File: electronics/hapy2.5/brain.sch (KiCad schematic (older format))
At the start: 37 parts, among them P10 WTemp probe, P11 LED Red Lower, P12 WCycle Lower, P13 WCycle Upper, P14 LED Red Upper, P15 Air probe, P16 LED White Upper, P17 LED White Lower, P19 Power button, P20 HE10-26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

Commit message: double check all component to footprint matches
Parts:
- Q6: footprint corecode:SOT-23-FET -> risebox:SOT-23-FET
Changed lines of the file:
@@
 F 0 "Q6" H 2710 1120 60  0000 R CNN
 F 1 "2N7002" H 2710 800 60  0000 R CNN
-F 2 "corecode:SOT-23-FET" H 2700 950 60  0001 C CNN
+F 2 "risebox:SOT-23-FET" H 2700 950 60  0001 C CNN
 F 3 "" H 2700 950 60  0000 C CNN
 	1    2700 950

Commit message: better borniers
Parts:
- removed P11: LED Red Lower, Connect:bornier2, symbol CONN_01X02
- removed P12: WCycle Lower, Connect:bornier2, symbol CONN_01X02
- removed P13: WCycle Upper, Connect:bornier2, symbol CONN_01X02
- removed P14: LED Red Upper, Connect:bornier2, symbol CONN_01X02
- removed P16: LED White Upper, Connect:bornier2, symbol CONN_01X02
- removed P17: LED White Lower, Connect:bornier2, symbol CONN_01X02
- removed P21: Multifunction button, Terminal_Blocks:TerminalBlock_WAGO-804_RM5mm_2pol, symbol CONN_01X02
- removed P22: Status light, Terminal_Blocks:TerminalBlock_WAGO-804_RM5mm_2pol, symbol CONN_01X02
- removed P6: WOverflow Lower, Connect:bornier2, symbol CONN_01X02
- removed P7: WOverflow Upper, Connect:bornier2, symbol CONN_01X02
- removed P8: LED Blue Lower, Connect:bornier2, symbol CONN_01X02
- removed P9: LED Blue Upper, Connect:bornier2, symbol CONN_01X02
- added P11: UPPER_BED, Connect:bornier4, symbol CONN_01X04
- added P6: UPPER_LEDS, Connect:bornier6, symbol CONN_01X06
- added P7: LOWER_LEDS, Connect:bornier6, symbol CONN_01X06
- added P8: USER_PANEL, Connect:bornier4, symbol CONN_01X04
- added P9: LOWER_BED, Connect:bornier4, symbol CONN_01X04
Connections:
- net GND: now also P11.2 (P2), P11.4 (P4), P6.2 (P2), P6.4 (P4), P6.6 (P6), P7.2 (P2), P7.4 (P4), P7.6 (P6), P8.2 (P2), P8.4 (P4), P9.2 (P2), P9.4 (P4)
- net P8_10: now also P11.3 (P3)
- net P8_32: now also P8.1 (P1)
- net P8_7: now also P9.3 (P3)
- net P8_8: now also P9.1 (P1)
- net P8_9: now also P11.1 (P1)
- net at R26.1: now also P6.1 (P1)
- net at R31.1: now also P6.3 (P3)
- net at R33.1: now also P6.5 (P5)
- net at R25.1: now also P7.1 (P1)
- net at R28.1: now also P7.3 (P3)
- net at R34.1: now also P7.5 (P5)
- net at R49.1: now also P8.3 (P3)
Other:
- note added: "Blue"
- note added: "Button"
- note added: "LOWER BED"
- note added: "LOWER LEDS"
- note added: "Overflow"
- note added: "Red"
- note added: "Status LED"
- note added: "UPPER BED"
- note added: "UPPER LEDS"
- note added: "USER PANEL"
- note added: "WCycle"
- note added: "White"
- moved on the sheet: P10, P15, R23, R24, R25, R26, R27, R28, R29, R30, R31, R32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

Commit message: power hackport with direct 5v vs bbb 5V
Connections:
- net 5VIn: now also P20.2, P20.24
- removed net 5V_EXT: P20.2, P20.24, U1.908 (SYS_5V)
- no-connect marks 36 -> 37
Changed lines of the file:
@@
 5V
 $Comp
-L GND #PWR30
+L GND #PWR030
 U 1 1 55F3CF20
 P 1250 7500
-F 0 "#PWR30" H 1250 7500 30  0001 C CNN
+F 0 "#PWR030" H 1250 7500 30  0001 C CNN
 F 1 "GND" H 1250 7430 30  0001 C CNN
 F 2 "" H 1250 7500 60  0000 C CNN
@@
 Text Label 3450 1350 2    60   ~ 0
 P9_23
-Text Label 7100 2150 2    60   ~ 0
-5V_EXT
 Text HLabel 1600 6550 0    60   Input ~ 0
 BatteryLevel
@@
 GND
 Text Label 3150 4050 2    60   ~ 0
-5V_EXT
+VDD_5V
 Text Label 1050 4150 0    60   ~ 0
 3.3V_EXT
@@
 GND
 Text Label 3150 5150 2    60   ~ 0
-5V_EXT
+VDD_5V
 Text Label 1050 5150 0    60   ~ 0
 3.3V_EXT
@@
 	6700 1550 7050 1550
 Wire Wire Line
-	6700 2150 7100 2150
-Wire Wire Line
 	6700 5950 7100 5950
 Wire Wire Line
@@
 Wire Wire Line
 	7100 4750 6700 4750
+NoConn ~ 6700 2150
 $EndSCHEMATC

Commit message: battery level pin is now AIN2
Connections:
- net BatteryLevel: now also U1.937 (AIN2); no longer R20.2, R21.1, U1.935 (AIN6)
- new net AIN6: R20.2, R21.1, U1.935 (AIN6)
- no-connect marks 37 -> 36
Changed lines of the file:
@@
 LIBS:memory
 LIBS:microchip
-LIBS:microchip1
 LIBS:microchip_pic10mcu
 LIBS:microchip_pic12mcu
@@
 LIBS:sensors
 LIBS:siliconi
-LIBS:special
 LIBS:stm8
 LIBS:stm32
@@
 BatteryLevel
 Text Label 2050 6550 2    60   ~ 0
-AIN6
+AIN2
 $Comp
 L HE10-26 P20
@@
 NoConn ~ 6700 4550
 NoConn ~ 6700 4650
-NoConn ~ 6700 5050
 NoConn ~ 6700 5150
 NoConn ~ 6700 5450
@@
 	7100 4750 6700 4750
 NoConn ~ 6700 2150
+Wire Wire Line
+	6700 5050 7100 5050
+Text Label 7100 5050 2    60   ~ 0
+AIN2
 $EndSCHEMATC

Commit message: routing P8 in progress
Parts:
- P10, P15: footprint Connect:bornier3 -> smisioto_bornier_mpt:mpt_0,5%2f3-2,54
- P11, P5, P8, P9: footprint Connect:bornier4 -> smisioto_bornier_mpt:mpt_0,5%2f4-2,54
- P19: footprint Connect:bornier2 -> smisioto_bornier_mpt:mpt_0,5%2f2-2,54
- P6, P7: footprint Connect:bornier6 -> smisioto_bornier_mpt:mpt_0,5%2f6-2,54
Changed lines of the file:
@@
 F 0 "P10" H 8300 5000 50  0000 C CNN
 F 1 "WTemp probe" V 8400 4800 50  0000 C CNN
-F 2 "Connect:bornier3" H 8300 4800 60  0001 C CNN
+F 2 "smisioto_bornier_mpt:mpt_0,5%2f3-2,54" H 8300 4800 60  0001 C CNN
 F 3 "" H 8300 4800 60  0000 C CNN
 	1    8300 4800
@@
 F 0 "P15" H 8350 2950 50  0000 C CNN
 F 1 "Air probe" V 8450 2750 50  0000 C CNN
-F 2 "Connect:bornier3" H 8350 2750 60  0001 C CNN
+F 2 "smisioto_bornier_mpt:mpt_0,5%2f3-2,54" H 8350 2750 60  0001 C CNN
 F 3 "" H 8350 2750 60  0000 C CNN
 	1    8350 2750
@@
 F 0 "P5" H 950 2550 50  0000 C CNN
 F 1 "Tank Level Sensor" V 1050 2300 50  0000 C CNN
-F 2 "Connect:bornier4" H 950 2300 60  0001 C CNN
+F 2 "smisioto_bornier_mpt:mpt_0,5%2f4-2,54" H 950 2300 60  0001 C CNN
 F 3 "" H 950 2300 60  0000 C CNN
 	1    950  2300
@@
 F 0 "P19" H 900 3200 50  0000 C CNN
 F 1 "Power button" V 1000 3050 50  0000 C CNN
-F 2 "Connect:bornier2" H 900 3050 60  0001 C CNN
+F 2 "smisioto_bornier_mpt:mpt_0,5%2f2-2,54" H 900 3050 60  0001 C CNN
 F 3 "" H 900 3050 60  0000 C CNN
 	1    900  3050
@@
 F 0 "P7" H 10600 6350 50  0000 C CNN
 F 1 "LOWER_LEDS" V 10700 6000 50  0000 C CNN
-F 2 "Connect:bornier6" H 10600 6000 60  0001 C CNN
+F 2 "smisioto_bornier_mpt:mpt_0,5%2f6-2,54" H 10600 6000 60  0001 C CNN
 F 3 "" H 10600 6000 60  0000 C CNN
 	1    10600 6000
@@
 F 0 "P6" H 10600 5200 50  0000 C CNN
 F 1 "UPPER_LEDS" V 10700 4850 50  0000 C CNN
-F 2 "Connect:bornier6" H 10600 4850 60  0001 C CNN
+F 2 "smisioto_bornier_mpt:mpt_0,5%2f6-2,54" H 10600 4850 60  0001 C CNN
 F 3 "" H 10600 4850 60  0000 C CNN
 	1    10600 4850
@@
 F 0 "P11" H 10800 3900 50  0000 C CNN
 F 1 "UPPER_BED" V 10900 3650 50  0000 C CNN
-F 2 "Connect:bornier4" H 10800 3650 60  0001 C CNN
+F 2 "smisioto_bornier_mpt:mpt_0,5%2f4-2,54" H 10800 3650 60  0001 C CNN
 F 3 "" H 10800 3650 60  0000 C CNN
 	1    10800 3650
@@
 F 0 "P9" H 10800 2700 50  0000 C CNN
 F 1 "LOWER_BED" V 10900 2450 50  0000 C CNN
-F 2 "Connect:bornier4" H 10800 2450 60  0001 C CNN
+F 2 "smisioto_bornier_mpt:mpt_0,5%2f4-2,54" H 10800 2450 60  0001 C CNN
 F 3 "" H 10800 2450 60  0000 C CNN
 	1    10800 2450
@@
 F 0 "P8" H 10800 1500 50  0000 C CNN
 F 1 "USER_PANEL" V 10900 1250 50  0000 C CNN
-F 2 "Connect:bornier4" H 10800 1250 60  0001 C CNN
+F 2 "smisioto_bornier_mpt:mpt_0,5%2f4-2,54" H 10800 1250 60  0001 C CNN
 F 3 "" H 10800 1250 60  0000 C CNN
 	1    10800 1250

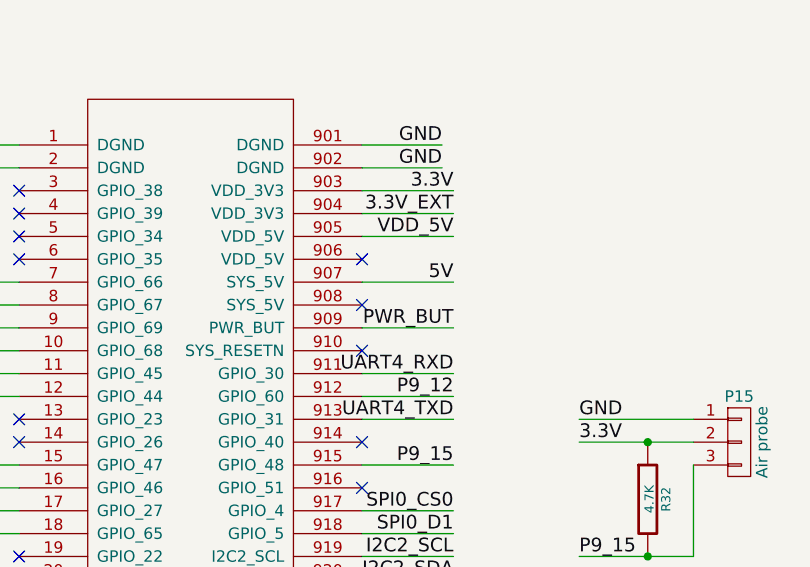
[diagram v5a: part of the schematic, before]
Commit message: all tracks to bbb and borniers are now backside plus avoid front and back tracks side by side
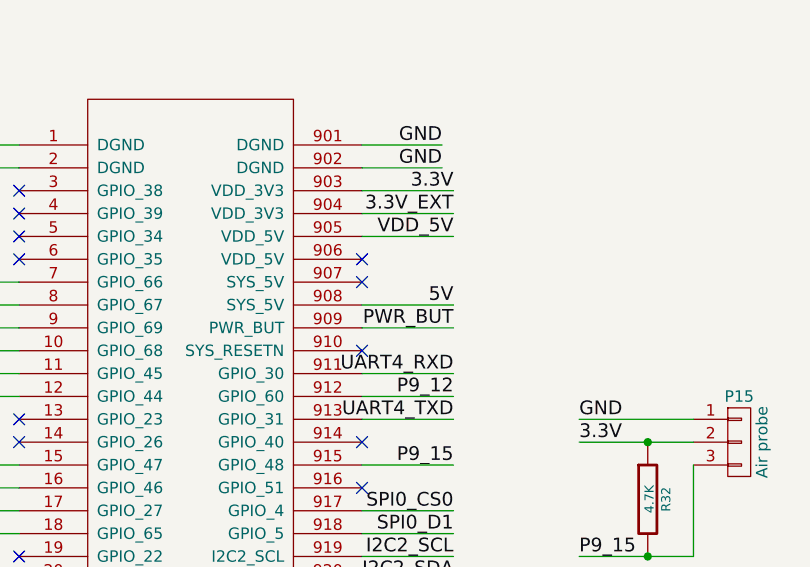
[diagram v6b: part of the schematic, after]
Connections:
- net 5V: now also U1.908 (SYS_5V); no longer U1.907 (SYS_5V)
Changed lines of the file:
@@
 LIBS:memory
 LIBS:microchip
+LIBS:microchip1
 LIBS:microchip_pic10mcu
 LIBS:microchip_pic12mcu
@@
 LIBS:sensors
 LIBS:siliconi
+LIBS:special
 LIBS:stm8
 LIBS:stm32
@@
 $Descr A4 11693 8268
 encoding utf-8
-Sheet 4 7
+Sheet 7 7
 Title ""
 Date ""
@@
 Text Label 7100 1650 2    60   ~ 0
 3.3V
-Text Label 7100 2050 2    60   ~ 0
+Text Label 7100 2150 2    60   ~ 0
 5V
 $Comp
-L GND #PWR030
+L GND #PWR035
 U 1 1 55F3CF20
 P 1250 7500
-F 0 "#PWR030" H 1250 7500 30  0001 C CNN
+F 0 "#PWR035" H 1250 7500 30  0001 C CNN
 F 1 "GND" H 1250 7430 30  0001 C CNN
 F 2 "" H 1250 7500 60  0000 C CNN
@@
 	6700 1650 7100 1650
 Wire Wire Line
-	6700 2050 7100 2050
-Wire Wire Line
 	1250 7500 1250 7250
 Wire Wire Line
@@
 Wire Wire Line
 	7100 4750 6700 4750
-NoConn ~ 6700 2150
 Wire Wire Line
 	6700 5050 7100 5050
 Text Label 7100 5050 2    60   ~ 0
 AIN2
+Wire Wire Line
+	6700 2150 7100 2150
+NoConn ~ 6700 2050
 $EndSCHEMATC

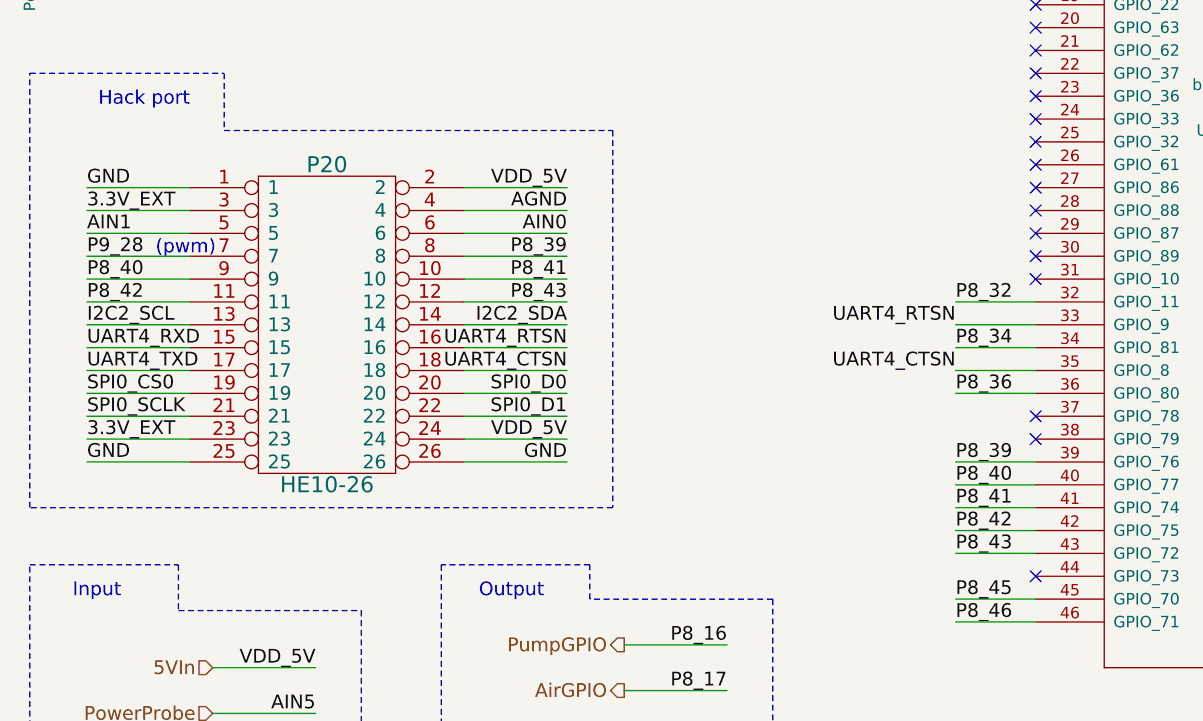
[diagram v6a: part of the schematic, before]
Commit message: route hackport and some alim twirks
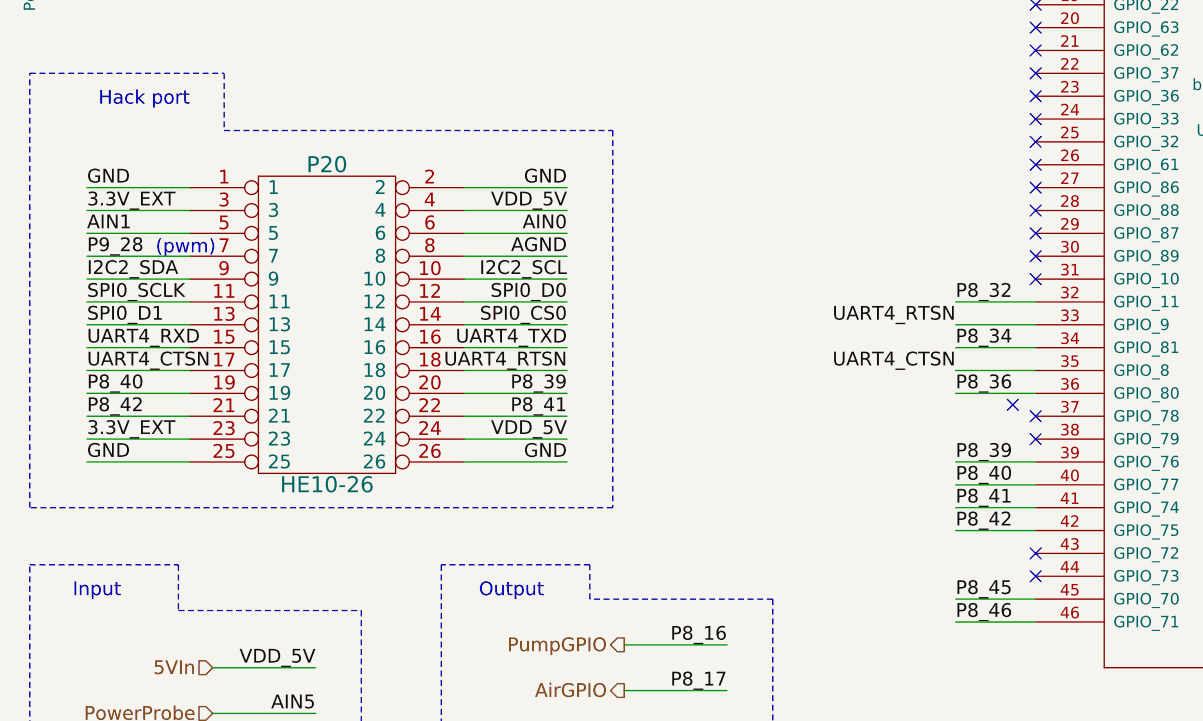
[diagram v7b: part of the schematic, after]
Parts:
- P20: footprint Connect:HE10_26D -> smisioto_he10:vasch_strip_13x2
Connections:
- net 5VIn: now also P20.4; no longer P20.2
- net AGND: now also P20.8; no longer P20.4
- net GND: now also P20.2
- net I2C2_SCL: now also P20.10; no longer P20.13
- net I2C2_SDA: now also P20.9; no longer P20.14
- net P8_39: now also P20.20; no longer P20.8
- net P8_40: now also P20.19; no longer P20.9
- net P8_41: now also P20.22; no longer P20.10
- net P8_42: now also P20.21; no longer P20.11
- net SPI0_CS0: now also P20.14; no longer P20.19
- net SPI0_D0: now also P20.12; no longer P20.20
- net SPI0_D1: now also P20.13; no longer P20.22
- net SPI0_SCLK: now also P20.11; no longer P20.21
- net UART4_CTSN: now also P20.17; no longer P20.18
- net UART4_RTSN: now also P20.18; no longer P20.16
- net UART4_TXD: now also P20.16; no longer P20.17
- net P8_43: no longer names the net of U1.43 (GPIO_72)
- net P8_43: no longer P20.12
- no-connect marks 36 -> 38
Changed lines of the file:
@@
 F 0 "P20" H 2100 5450 70  0000 C CNN
 F 1 "HE10-26" H 2100 4050 70  0000 C CNN
-F 2 "Connect:HE10_26D" H 2100 4700 60  0001 C CNN
+F 2 "smisioto_he10:vasch_strip_13x2" H 2100 4700 60  0001 C CNN
 F 3 "" H 2100 4700 60  0000 C CNN
 	1    2100 4700
@@
 Text Label 1050 4050 0    60   ~ 0
 GND
-Text Label 3150 4050 2    60   ~ 0
+Text Label 3150 4150 2    60   ~ 0
 VDD_5V
 Text Label 1050 4150 0    60   ~ 0
@@
 Text Label 3150 4250 2    60   ~ 0
 AIN0
-Text Label 3150 4150 2    60   ~ 0
+Text Label 3150 4350 2    60   ~ 0
 AGND
 Text Label 1050 4250 0    60   ~ 0
@@
 Text Label 1050 4350 0    60   ~ 0
 P9_28
-Text Label 3150 4350 2    60   ~ 0
+Text Label 3150 4950 2    60   ~ 0
 P8_39
-Text Label 1050 4450 0    60   ~ 0
+Text Label 1050 4950 0    60   ~ 0
 P8_40
-Text Label 3150 4450 2    60   ~ 0
+Text Label 3150 5050 2    60   ~ 0
 P8_41
-Text Label 1050 4550 0    60   ~ 0
+Text Label 1050 5050 0    60   ~ 0
 P8_42
-Text Label 3150 4550 2    60   ~ 0
-P8_43
 Text Notes 1350 4350 0    60   ~ 0
 (pwm)
-Text Label 1050 4650 0    60   ~ 0
+Text Label 3150 4450 2    60   ~ 0
 I2C2_SCL
-Text Label 3150 4650 2    60   ~ 0
+Text Label 1050 4450 0    60   ~ 0
 I2C2_SDA
 Text Label 1050 4750 0    60   ~ 0
 UART4_RXD
+Text Label 3150 4750 2    60   ~ 0
+UART4_TXD
+Text Label 3150 4850 2    60   ~ 0
+UART4_RTSN
 Text Label 1050 4850 0    60   ~ 0
-UART4_TXD
-Text Label 3150 4750 2    60   ~ 0
-UART4_RTSN
-Text Label 3150 4850 2    60   ~ 0
 UART4_CTSN
-Text Label 1050 4950 0    60   ~ 0
+Text Label 3150 4650 2    60   ~ 0
 SPI0_CS0
-Text Label 3150 4950 2    60   ~ 0
+Text Label 3150 4550 2    60   ~ 0
 SPI0_D0
-Text Label 3150 5050 2    60   ~ 0
+Text Label 1050 4650 0    60   ~ 0
 SPI0_D1
-Text Label 1050 5050 0    60   ~ 0
+Text Label 1050 4550 0    60   ~ 0
 SPI0_SCLK
 Text Label 4850 5250 0    60   ~ 0
@@
 Text Label 4850 5450 0    60   ~ 0
 P8_41
-Text Label 4850 5650 0    60   ~ 0
-P8_43
 Text Label 4850 5350 0    60   ~ 0
 P8_40
@@
 	5200 5450 4850 5450
 Wire Wire Line
-	5200 5650 4850 5650
-Wire Wire Line
 	5200 5350 4850 5350
 Wire Wire Line
@@
 	6700 2150 7100 2150
 NoConn ~ 6700 2050
+Text Label 3150 4050 2    60   ~ 0
+GND
+NoConn ~ 5200 5650
+NoConn ~ 5100 5000
 $EndSCHEMATC

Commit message: gerbers plus repaired pcb
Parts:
- P20: value HE10-26 -> T821126A1S100CEU HE10-26
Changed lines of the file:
@@
 P 2100 4700
 F 0 "P20" H 2100 5450 70  0000 C CNN
-F 1 "HE10-26" H 2100 4050 70  0000 C CNN
+F 1 "T821126A1S100CEU  HE10-26" H 2100 4050 70  0000 C CNN
 F 2 "smisioto_he10:vasch_strip_13x2" H 2100 4700 60  0001 C CNN
 F 3 "" H 2100 4700 60  0000 C CNN
